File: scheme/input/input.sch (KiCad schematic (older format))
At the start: 5 parts, among them U1 TL431ACZ

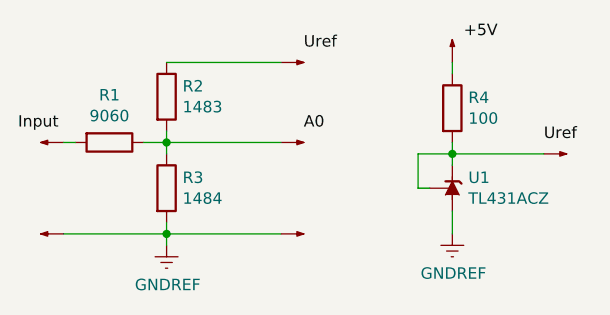
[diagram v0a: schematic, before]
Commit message: Обновлена схема подключения
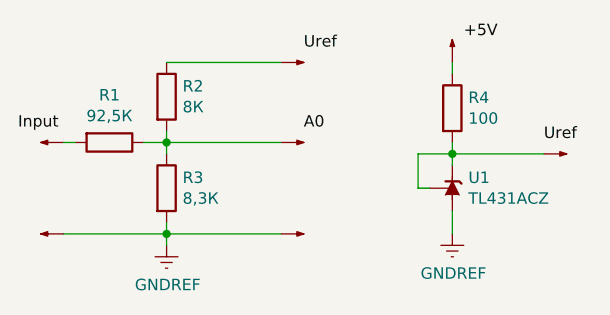
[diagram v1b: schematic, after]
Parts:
- R1: value 9060 -> 92,5К
- R2: value 1483 -> 8К
- R3: value 1484 -> 8,3К
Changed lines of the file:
@@
 P 1550 2400
 F 0 "R3" H 1620 2446 50  0000 L CNN
-F 1 "1484" H 1620 2355 50  0000 L CNN
+F 1 "8,3К" H 1620 2355 50  0000 L CNN
 F 2 "" V 1480 2400 50  0001 C CNN
 F 3 "~" H 1550 2400 50  0001 C CNN
@@
 P 1550 2000
 F 0 "R2" H 1620 2046 50  0000 L CNN
-F 1 "1483" H 1620 1955 50  0000 L CNN
+F 1 "8К" H 1620 1955 50  0000 L CNN
 F 2 "" V 1480 2000 50  0001 C CNN
 F 3 "~" H 1550 2000 50  0001 C CNN
@@
 P 1300 2200
 F 0 "R1" V 1093 2200 50  0000 C CNN
-F 1 "9060" V 1184 2200 50  0000 C CNN
+F 1 "92,5К" V 1184 2200 50  0000 C CNN
 F 2 "" V 1230 2200 50  0001 C CNN
 F 3 "~" H 1300 2200 50  0001 C CNN
